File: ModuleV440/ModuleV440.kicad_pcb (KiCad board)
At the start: 2 copper layers, 30 x 61.3 mm, 45 parts, among them J2 AVR-ISP-6, Q1 AO3400A, U1 EL3H7(B)(TA)-G, Y1 8MHZ Ceramic Resonator

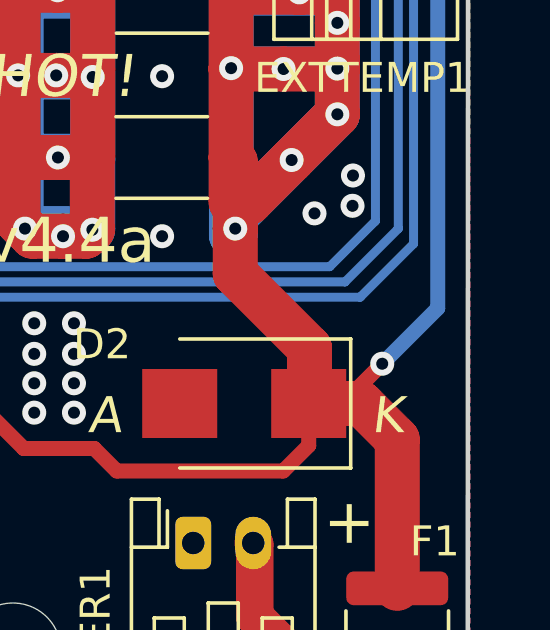
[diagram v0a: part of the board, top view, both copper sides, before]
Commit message: Add hash to Module440 board
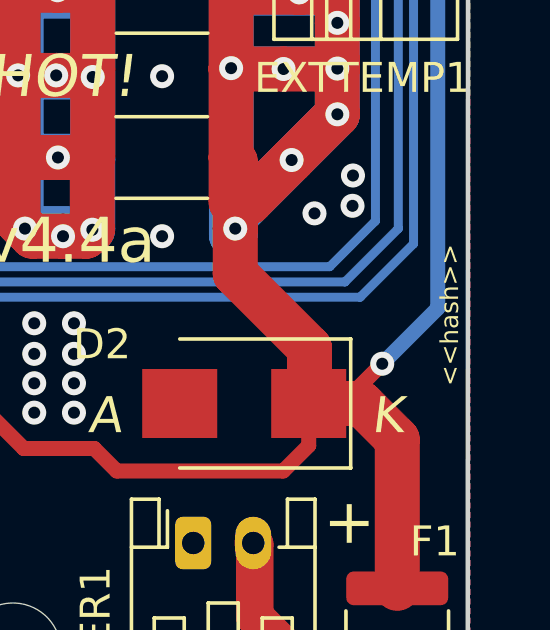
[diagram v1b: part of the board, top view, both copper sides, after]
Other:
- board text added: "<<hash>>"
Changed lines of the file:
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@@
     (effects (font (size 1.5 1.5) (thickness 0.3)))
+  )
+  (gr_text "<<hash>>" (at 131.3176 94.4376 90) (layer "F.SilkS")
+    (effects (font (size 0.6 0.6) (thickness 0.09)))
   )
   (dimension (type aligned) (layer "Dwgs.User")

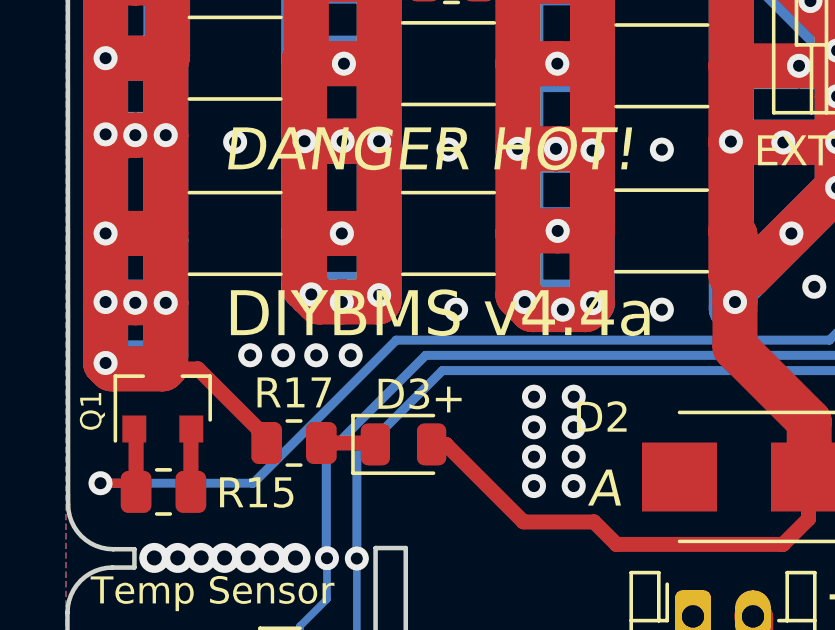
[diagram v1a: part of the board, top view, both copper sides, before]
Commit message: Rename Module 440 to 441
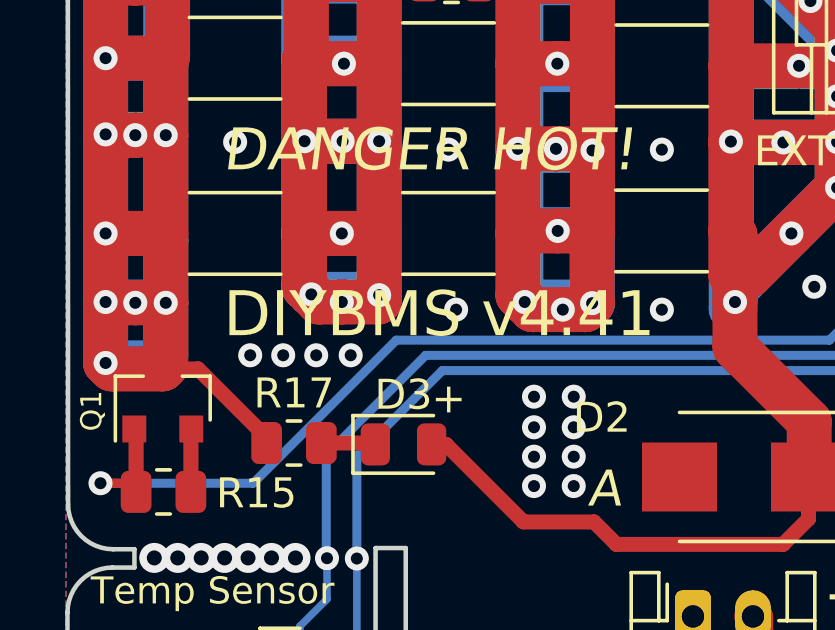
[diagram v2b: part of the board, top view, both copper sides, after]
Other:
- board text added: "DIYBMS v4.41"
- board text removed: "DIYBMS v4.4a"
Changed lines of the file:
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@@
     (effects (font (size 0.7 0.7) (thickness 0.175)))
   )
-  (gr_text "DIYBMS v4.4a" (at 121.5076 91.9676) (layer "F.SilkS")
+  (gr_text "DIYBMS v4.41" (at 121.5076 91.9676) (layer "F.SilkS")
     (effects (font (size 1.5 1.5) (thickness 0.35)) (justify right))
   )
